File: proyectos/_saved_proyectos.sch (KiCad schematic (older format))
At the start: 54 parts, among them P1 CONN_01X06, P2 CONN_01X03, P3 CONN_01X05, P4 CONN_01X04, SW1 SW_PUSH, U1 AD8232_A, U2 ADP3339, U3 PIC16F688, Y1 Crystal_8MHz

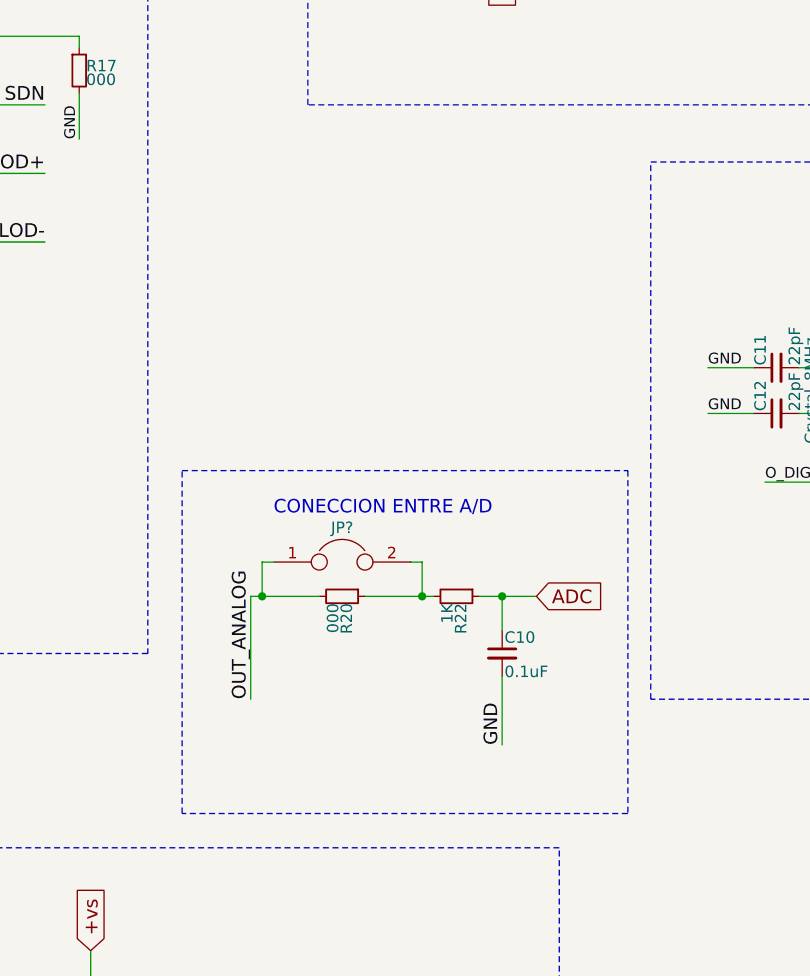
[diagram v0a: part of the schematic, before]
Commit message: version ECG 1.3
MODIFICACION DE ESQUEMATICO
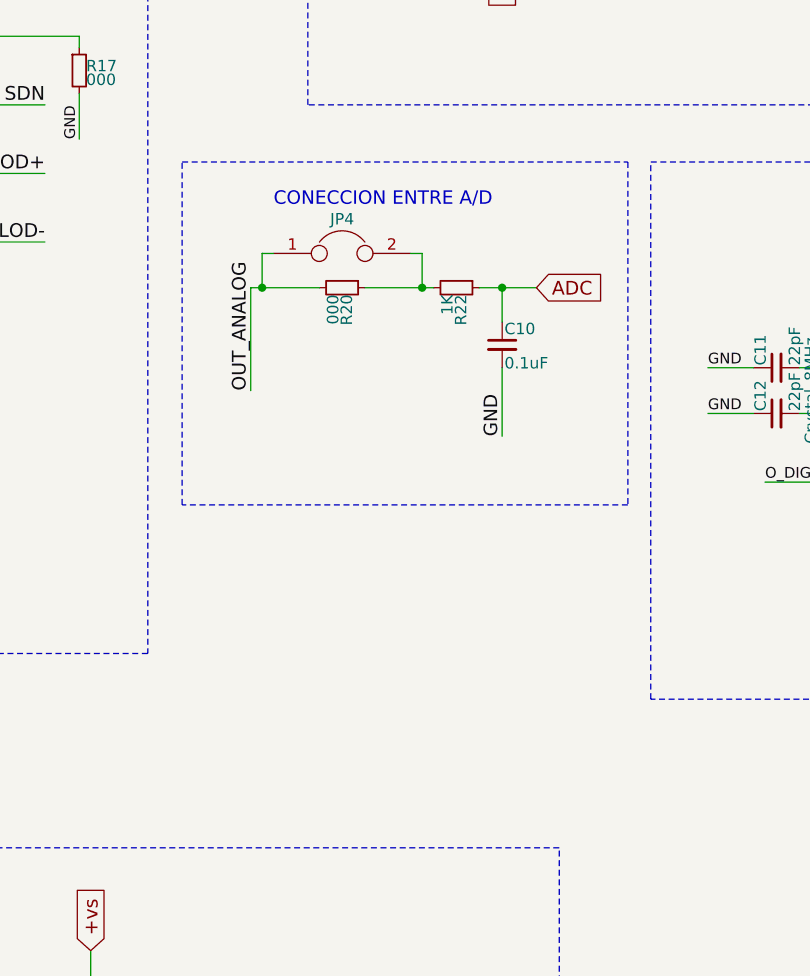
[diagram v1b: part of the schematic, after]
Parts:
- JP2, JP3: footprint (none) -> Pin_Headers:Pin_Header_Straight_1x02_Pitch2.54mm
- JP4: renamed from JP?; footprint (none) -> Pin_Headers:Pin_Header_Straight_1x02_Pitch2.54mm
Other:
- moved on the sheet: C10, JP4, R20, R22
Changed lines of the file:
@@
 Text GLabel 7650 1800 3    60   Input ~ 0
 +vs
-Text GLabel 6650 4900 2    60   Input ~ 0
+Text GLabel 6650 3550 2    60   Input ~ 0
 ADC
 $Comp
@@
 L 0.1uF C10
 U 1 1 5913BE16
-P 6500 5150
-F 0 "C10" H 6510 5220 50  0000 L CNN
-F 1 "0.1uF" H 6510 5070 50  0000 L CNN
-F 2 "Capacitors_SMD:C_0805_HandSoldering" H 6410 5120 50  0001 C CNN
-F 3 "" H 6510 5220 50  0000 C CNN
-F 4 "1276-2450-2-ND" H 6610 5320 60  0001 C CNN "CAP CER 0.1UF 25V X7R 0805"
-	1    6500 5150
+P 6500 3800
+F 0 "C10" H 6510 3870 50  0000 L CNN
+F 1 "0.1uF" H 6510 3720 50  0000 L CNN
+F 2 "Capacitors_SMD:C_0805_HandSoldering" H 6410 3770 50  0001 C CNN
+F 3 "" H 6510 3870 50  0000 C CNN
+F 4 "1276-2450-2-ND" H 6610 3970 60  0001 C CNN "CAP CER 0.1UF 25V X7R 0805"
+	1    6500 3800
 	1    0    0    -1
 $EndComp
@@
 L 000 R20
 U 1 1 59142595
-P 5800 4900
-F 0 "R20" H 5830 4920 50  0000 L CNN
-F 1 "000" H 5830 4860 50  0000 L CNN
-F 2 "Resistors_SMD:R_0805_HandSoldering" H 5730 4820 50  0001 C CNN
-F 3 "" H 5830 4920 50  0000 C CNN
-F 4 "311-0.0ARTR-ND" H 5930 5020 60  0001 C CNN "RES SMD 0.0 OHM JUMPER 1/8W 0805"
-	1    5800 4900
+P 5800 3550
+F 0 "R20" H 5830 3570 50  0000 L CNN
+F 1 "000" H 5830 3510 50  0000 L CNN
+F 2 "Resistors_SMD:R_0805_HandSoldering" H 5730 3470 50  0001 C CNN
+F 3 "" H 5830 3570 50  0000 C CNN
+F 4 "311-0.0ARTR-ND" H 5930 3670 60  0001 C CNN "RES SMD 0.0 OHM JUMPER 1/8W 0805"
+	1    5800 3550
 	0    1    1    0
 $EndComp
@@
 L 1K R22
 U 1 1 591446F7
-P 6300 4900
-F 0 "R22" H 6330 4920 50  0000 L CNN
-F 1 "1K" H 6330 4860 50  0000 L CNN
-F 2 "Resistors_SMD:R_0805_HandSoldering" H 6230 4820 50  0001 C CNN
-F 3 "" H 6300 4900 50  0000 C CNN
-F 4 "RMCF0805FT1K00TR-ND" H 6430 5020 60  0001 C CNN "RES SMD 1K OHM 1% 1/8W 0805"
-	1    6300 4900
+P 6300 3550
+F 0 "R22" H 6330 3570 50  0000 L CNN
+F 1 "1K" H 6330 3510 50  0000 L CNN
+F 2 "Resistors_SMD:R_0805_HandSoldering" H 6230 3470 50  0001 C CNN
+F 3 "" H 6300 3550 50  0000 C CNN
+F 4 "RMCF0805FT1K00TR-ND" H 6430 3670 60  0001 C CNN "RES SMD 1K OHM 1% 1/8W 0805"
+	1    6300 3550
 	0    1    1    0
 $EndComp
@@
 	3400 4700 3700 4700
 Wire Wire Line
-	6500 4900 6500 5050
-Connection ~ 6500 4900
-Wire Wire Line
-	6500 5250 6500 5550
+	6500 3550 6500 3700
+Connection ~ 6500 3550
+Wire Wire Line
+	6500 3900 6500 4200
 Wire Wire Line
 	2000 2450 1800 2450
@@
 GND
 Wire Notes Line
-	5100 4350 7050 4350
-Wire Notes Line
-	7050 4350 7050 5850
-Wire Notes Line
-	7050 5850 5100 5850
-Wire Notes Line
-	5100 5850 5100 4350
-Text Label 5400 5350 1    60   ~ 0
+	5100 3000 7050 3000
+Wire Notes Line
+	7050 3000 7050 4500
+Wire Notes Line
+	7050 4500 5100 4500
+Wire Notes Line
+	5100 4500 5100 3000
+Text Label 5400 4000 1    60   ~ 0
 OUT_ANALOG
-Text Notes 5500 4550 0    59   ~ 0
+Text Notes 5500 3200 0    59   ~ 0
 CONECCION ENTRE A/D\n
 Wire Notes Line
@@
 Text Notes 850  4950 0    59   ~ 0
 BLOQUE DE ADQUISICION DE ECG
-Text Label 6500 5550 1    59   ~ 0
+Text Label 6500 4200 1    59   ~ 0
 GND
 Wire Wire Line
@@
 F 0 "JP2" H 6250 1800 50  0000 C CNN
 F 1 "JUMPER" H 6250 1570 50  0001 C CNN
-F 2 "" H 6250 1650 50  0000 C CNN
+F 2 "Pin_Headers:Pin_Header_Straight_1x02_Pitch2.54mm" H 6250 1650 50  0001 C CNN
 F 3 "" H 6250 1650 50  0000 C CNN
 	1    6250 1650
@@
 F 0 "JP3" H 6750 1800 50  0000 C CNN
 F 1 "JUMPER" H 6750 1570 50  0001 C CNN
-F 2 "" H 6750 1650 50  0000 C CNN
+F 2 "Pin_Headers:Pin_Header_Straight_1x02_Pitch2.54mm" H 6750 1650 50  0001 C CNN
 F 3 "" H 6750 1650 50  0000 C CNN
 	1    6750 1650
@@
 CONVERTIDOR ANALOGICO A DIGITAL\n
 $Comp
-L JUMPER JP?
+L JUMPER JP4
 U 1 1 5915CB88
-P 5800 4750
-F 0 "JP?" H 5800 4900 50  0000 C CNN
-F 1 "JUMPER" H 5800 4670 50  0001 C CNN
-F 2 "" H 5800 4750 50  0000 C CNN
-F 3 "" H 5800 4750 50  0000 C CNN
-	1    5800 4750
-	1    0    0    -1
-$EndComp
-Wire Wire Line
-	6650 4900 6400 4900
-Wire Wire Line
-	5900 4900 6200 4900
-Wire Wire Line
-	6100 4750 6150 4750
-Wire Wire Line
-	6150 4750 6150 4900
-Connection ~ 6150 4900
-Wire Wire Line
-	5500 4750 5450 4750
-Wire Wire Line
-	5450 4750 5450 4900
-Connection ~ 5450 4900
-Wire Wire Line
-	5400 4900 5700 4900
-Wire Wire Line
-	5400 4900 5400 5350
+P 5800 3400
+F 0 "JP4" H 5800 3550 50  0000 C CNN
+F 1 "JUMPER" H 5800 3320 50  0001 C CNN
+F 2 "Pin_Headers:Pin_Header_Straight_1x02_Pitch2.54mm" H 5800 3400 50  0001 C CNN
+F 3 "" H 5800 3400 50  0000 C CNN
+	1    5800 3400
+	1    0    0    -1
+$EndComp
+Wire Wire Line
+	6650 3550 6400 3550
+Wire Wire Line
+	5900 3550 6200 3550
+Wire Wire Line
+	6100 3400 6150 3400
+Wire Wire Line
+	6150 3400 6150 3550
+Connection ~ 6150 3550
+Wire Wire Line
+	5500 3400 5450 3400
+Wire Wire Line
+	5450 3400 5450 3550
+Connection ~ 5450 3550
+Wire Wire Line
+	5400 3550 5700 3550
+Wire Wire Line
+	5400 3550 5400 4000
 $EndSCHEMATC

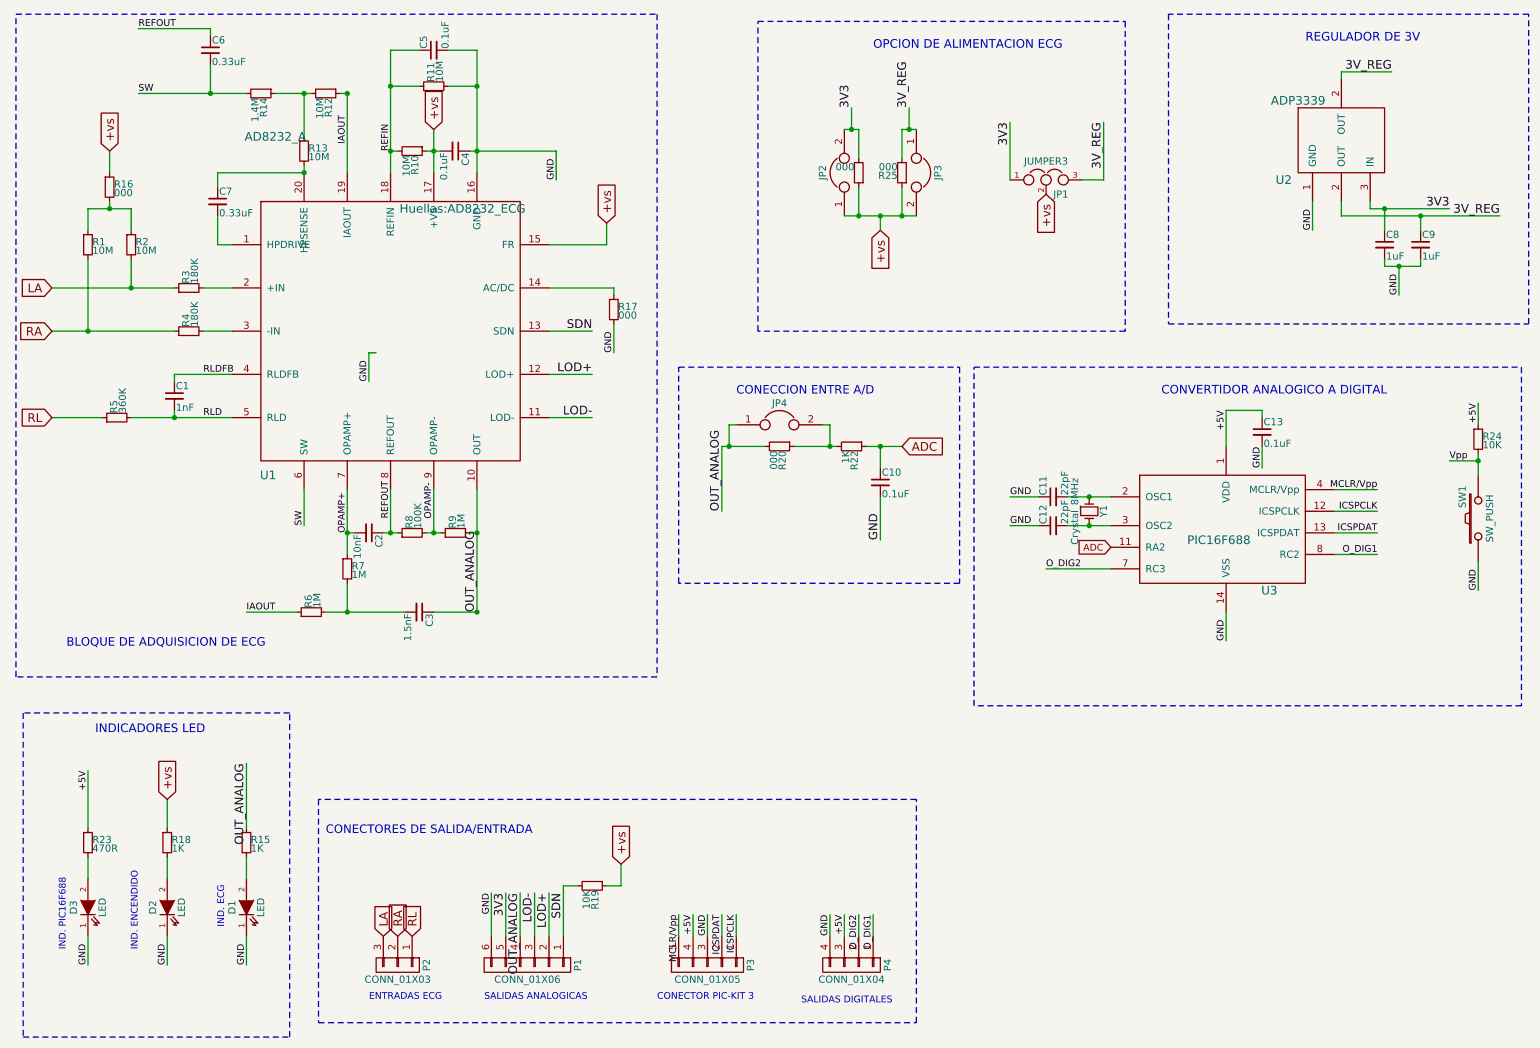
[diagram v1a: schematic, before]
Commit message: version ECG 1.4
INCORPORACION DE PIC Y REGULADOR
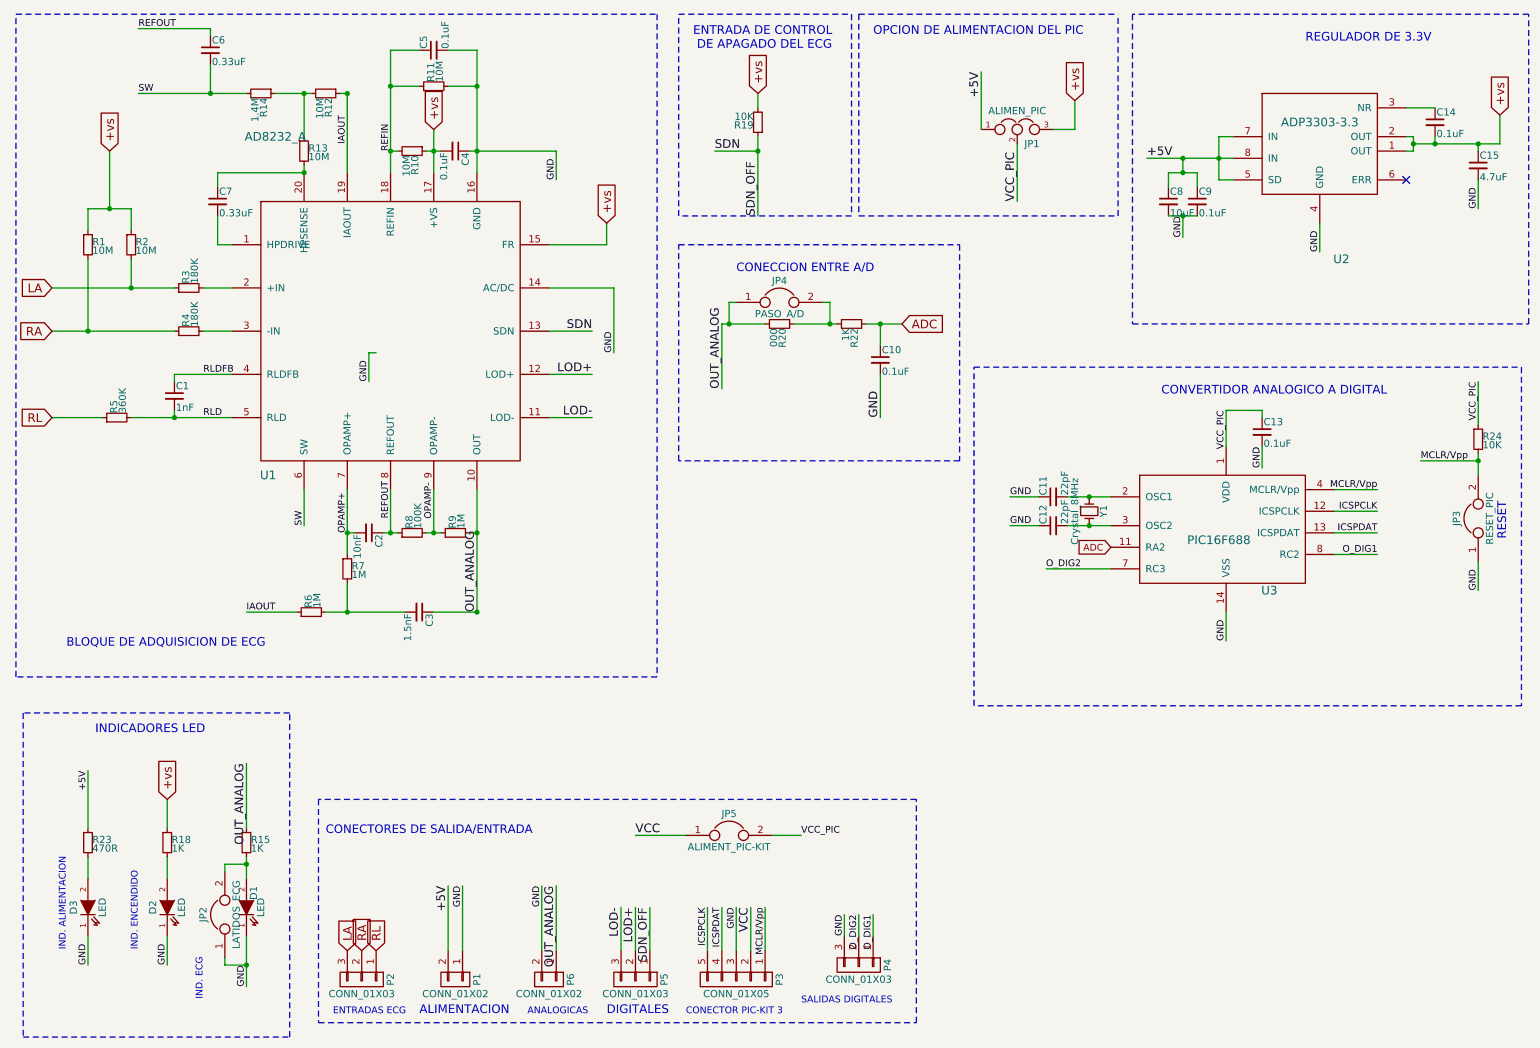
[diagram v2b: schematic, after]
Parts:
- removed C8, C9: 1uF, Capacitors_SMD:C_0805_HandSoldering, symbol 1uF
- removed JP2, JP3, JP4: JUMPER, Pin_Headers:Pin_Header_Straight_1x02_Pitch2.54mm, symbol JUMPER
- removed P1: CONN_01X06, Huellas:Pin_Header_Straight_1x06_Pitch2.54mm, symbol CONN_01X06
- removed P4: CONN_01X04, Pin_Headers:Pin_Header_Straight_1x04_Pitch2.54mm, symbol CONN_01X04
- removed R16, R17, R21, R25: 000, Resistors_SMD:R_0805_HandSoldering, symbol 000
- removed SW1: SW_PUSH, Huellas:SWICHT_KPT-1187B, symbol SW_PUSH
- removed U2: ADP3339, TO_SOT_Packages_SMD:SOT-223-3Lead_TabPin2, symbol ADP3339
- added C14, C9: 0.1uF, Capacitors_SMD:C_0805_HandSoldering, symbol 0.1uF
- added C15: 4.7uF, Capacitors_SMD:C_0805_HandSoldering, symbol 4.7uF
- added C8: 10uF, Capacitors_SMD:C_0805_HandSoldering, symbol 10uF
- added JP2: LATIDOS_ECG, Pin_Headers:Pin_Header_Straight_1x02_Pitch2.54mm, symbol LATIDOS_ECG
- added JP3: RESET_PIC, Pin_Headers:Pin_Header_Straight_1x02_Pitch2.54mm, symbol RESET_PIC
- added JP4: PASO_A/D, Pin_Headers:Pin_Header_Straight_1x02_Pitch2.54mm, symbol PASO_A/D
- added JP5: ALIMENT_PIC-KIT, Pin_Headers:Pin_Header_Straight_1x02_Pitch2.54mm, symbol ALIMENT_PIC-KIT
- added P1, P6: CONN_01X02, Pin_Headers:Pin_Header_Straight_1x02_Pitch2.54mm, symbol CONN_01X02
- added P4: CONN_01X03, Pin_Headers:Pin_Header_Straight_1x03_Pitch2.54mm, symbol CONN_01X03
- added P5: CONN_01X03, Pin_Headers:Pin_Header_Straight_1x03_Pitch2.54mm, symbol CONN_01X03-RESCUE-proyectos
- added U2: ADP3303-3.3, Housings_SOIC:SOIC-8_3.9x4.9mm_Pitch1.27mm, symbol ADP3303-3.3
- JP1: value JUMPER3 -> ALIMEN_PIC; footprint (none) -> Pin_Headers:Pin_Header_Straight_1x03_Pitch2.54mm
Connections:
- net 3V3 is gone; now on net +5V: JP1.1
- net 3V_REG is gone; now on net +vs: JP1.3
- net Vpp is gone; now on net MCLR/Vpp: R24.2
- net +5V: now also C8.1, C9.1, P1.2 (P2), U2.5 (SD), U2.7 (IN), U2.8 (IN); no longer C13.1, P3.4 (P4), R24.1, U3.1 (VDD)
- net +vs: now also R1.1, R19.2, R2.1, C14.2, C15.1, U2.1 (OUT), U2.2 (OUT); no longer JP1.2, R19.1
- net GND: now also U1.14 (AC/DC), C15.2, C8.2, C9.2, JP2.1, JP3.1, P1.1 (P1), P4.3 (P3), P6.2 (P2), U2.4 (GND)
- net ICSPCLK: now also P3.5 (P5); no longer P3.1 (P1)
- net ICSPDAT: now also P3.4 (P4); no longer P3.2 (P2)
- net LOD+: now also P5.2 (LA)
- net LOD-: now also P5.3 (RA)
- net MCLR/Vpp: now also P3.1 (P1), JP3.2; no longer P3.5 (P5)
- net OUT_ANALOG: now also JP4.1, P6.1 (P1)
- net O_DIG1: now also P4.1 (P1)
- net O_DIG2: now also P4.2 (P2)
- net SDN: now also R19.1, P5.1 (RL); no longer R19.2
- net at D1.2 (A), R15.2: now also JP2.2
- net at R20.1, R22.2: now also JP4.2
- new net: C14.1, U2.3 (NR)
- new net VCC: JP5.1, P3.2 (P2)
- new net VCC_PIC: C13.1, JP1.2, JP5.2, R24.1, U3.1 (VDD)
- no-connect marks 0 -> 1
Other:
- note added: "ALIMENTACION\n"
- note added: "ANALOGICAS\n"
- note added: "DIGITALES\n"
- note added: "ENTRADA DE CONTROL\n DE APAGADO DEL ECG"
- note added: "IND. ALIMENTACION\n"
- note added: "OPCION DE ALIMENTACION DEL PIC\n\n"
- note added: "REGULADOR DE 3.3V\n"
- note added: "RESET"
- note removed: "IND. PIC16F688"
- note removed: "OPCION DE ALIMENTACION ECG\n"
- note removed: "REGULADOR DE 3V\n"
- note removed: "SALIDAS ANALOGICAS\n"
- moved on the sheet: C10, JP1, P2, P3, R19, R20, R22
